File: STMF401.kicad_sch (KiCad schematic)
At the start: 26 parts, among them J6 Conn_01x04_Pin, U3 STM32F407VETx, Y1 X322525MQB4SI, Y2 SMD03215C2

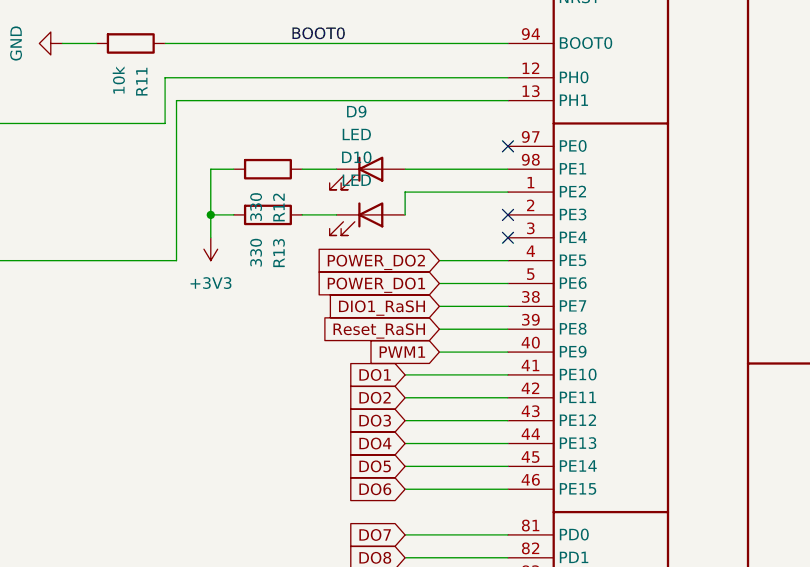
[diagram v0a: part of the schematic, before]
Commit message: feat: разведены сигналньные линии для приёмо-передатчиков LoRa и LoRa_SH
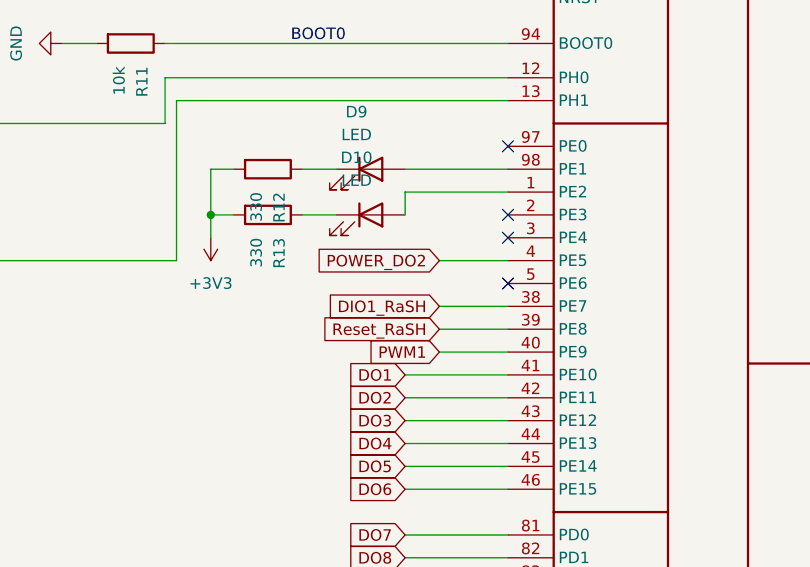
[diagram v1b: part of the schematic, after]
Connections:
- net POWER_DO1: no longer names the net of U3.5 (PE6)
- no-connect marks 20 -> 21
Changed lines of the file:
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@@
+	)
+	(no_connect
+		(at 177.8 91.44)
 	)
 	(no_connect
@@
 	(wire
 		(pts
-			(xy 170.18 91.44) (xy 177.8 91.44)
-		)
-		(stroke
-			(width 0)
-			(type default)
-		)
-	)
-	(wire
-		(pts
 			(xy 260.35 92.71) (xy 278.13 92.71)
 		)
@@
 			(hide yes)
 			(show_name no)
-			(do_not_autoplace no)
-			(effects
-				(font
-					(size 1.27 1.27)
-				)
-				(justify right)
-			)
-		)
-	)
-	(global_label "POWER_DO1"
-		(shape input)
-		(at 170.18 91.44 180)
-		(fields_autoplaced yes)
-		(effects
-			(font
-				(size 1.27 1.27)
-			)
-			(justify right)
-		)
-		(property "Intersheetrefs" "${INTERSHEET_REFS}"
-			(at 155.9463 91.44 0)
-			(hide yes)
-			(show_name no)

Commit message: feat: разведены линии DI большая часть
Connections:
- net DI10: now also U3.57 (PD10); no longer U3.60 (PD13)
- net DI11: now also U3.56 (PD9); no longer U3.61 (PD14)
- net DI12: now also U3.55 (PD8); no longer U3.62 (PD15)
- net DI5: now also U3.62 (PD15); no longer U3.55 (PD8)
- net DI6: now also U3.61 (PD14); no longer U3.56 (PD9)
- net DI7: now also U3.60 (PD13); no longer U3.57 (PD10)
- net DI8: now also U3.59 (PD12); no longer U3.58 (PD11)
- net DI9: now also U3.58 (PD11); no longer U3.59 (PD12)
- net DO10: now also U3.81 (PD0); no longer U3.84 (PD3)
- net DO7: now also U3.84 (PD3); no longer U3.81 (PD0)
- net DO8: now also U3.83 (PD2); no longer U3.82 (PD1)
- net DO9: now also U3.82 (PD1); no longer U3.83 (PD2)
